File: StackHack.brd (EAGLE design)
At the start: 18.3 x 7.9 mm, 0 parts

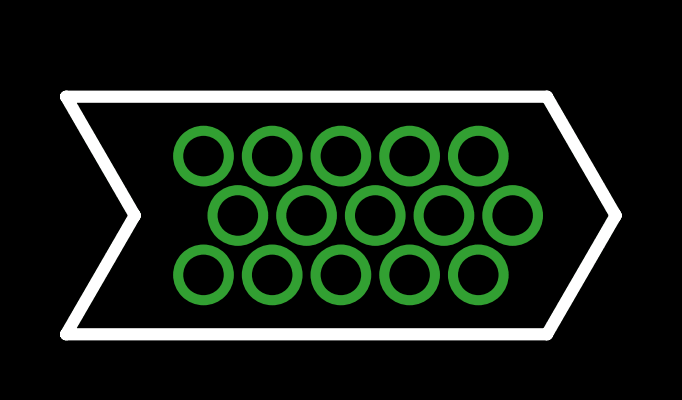
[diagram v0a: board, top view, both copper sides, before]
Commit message: Two VGA's at the same time
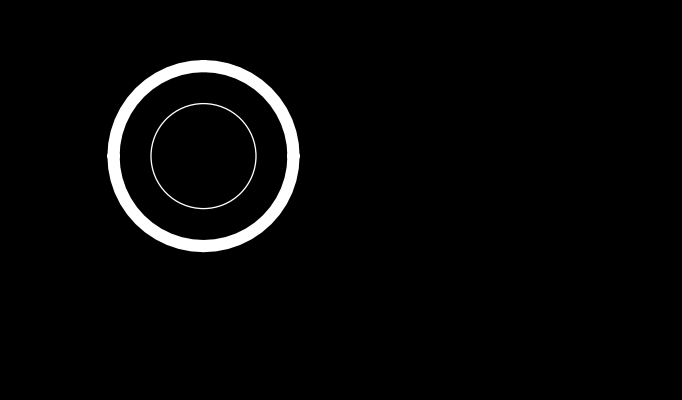
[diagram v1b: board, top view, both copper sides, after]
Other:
- board size 18.3 x 7.9 mm -> 6 x 6 mm
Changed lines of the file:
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@@
 <setting verticaltext="up"/>
 </settings>
-<grid distance="1.98" unitdist="mm" unit="mm" style="lines" multiple="1" display="yes" altdistance="1.98" altunitdist="mm" altunit="mm"/>
+<grid distance="0.5" unitdist="mm" unit="mm" style="lines" multiple="2" display="yes" altdistance="0.1" altunitdist="mm" altunit="mm"/>
 <layers>
 <layer number="1" name="Top" color="4" fill="1" visible="yes" active="yes"/>
@@
 <layer number="43" name="vRestrict" color="2" fill="10" visible="yes" active="yes"/>
 <layer number="44" name="Drills" color="7" fill="1" visible="no" active="yes"/>
-<layer number="45" name="Holes" color="7" fill="1" visible="no" active="yes"/>
+<layer number="45" name="Holes" color="7" fill="1" visible="yes" active="yes"/>
 <layer number="46" name="Milling" color="3" fill="1" visible="no" active="yes"/>
 <layer number="47" name="Measures" color="7" fill="1" visible="no" active="yes"/>
@@
 <board>
 <plain>
-<wire x1="-2.29" y1="-1.98" x2="-4.58" y2="-5.94" width="0.4064" layer="20"/>
-<wire x1="-4.58" y1="1.98" x2="-2.29" y2="-1.98" width="0.4064" layer="20"/>
-<wire x1="13.74" y1="-1.98" x2="11.45" y2="-5.94" width="0.4064" layer="20"/>
-<wire x1="11.45" y1="1.98" x2="13.74" y2="-1.98" width="0.4064" layer="20"/>
-<wire x1="-4.58" y1="1.98" x2="11.45" y2="1.98" width="0.4064" layer="20"/>
-<wire x1="-4.58" y1="-5.94" x2="11.45" y2="-5.94" width="0.4064" layer="20"/>
+<hole x="0" y="0" drill="3.5"/>
+<wire x1="3" y1="0" x2="0" y2="3" width="0.4064" layer="20" curve="90"/>
+<wire x1="0" y1="3" x2="-3" y2="0" width="0.4064" layer="20" curve="90"/>
+<wire x1="-3" y1="0" x2="0" y2="-3" width="0.4064" layer="20" curve="90"/>
+<wire x1="0" y1="-3" x2="3" y2="0" width="0.4064" layer="20" curve="90"/>
 </plain>
 <attributes>
@@
 </elements>
 <signals>
-<signal name="S$1">
-<via x="0" y="0" extent="1-16" drill="1.35"/>
-</signal>
-<signal name="S$2">
-<via x="1.145" y="-1.98" extent="1-16" drill="1.35"/>
-</signal>
-<signal name="S$3">
-<via x="0" y="-3.96" extent="1-16" drill="1.35"/>
-</signal>
-<signal name="S$4">
-<via x="2.29" y="0" extent="1-16" drill="1.35"/>
-</signal>
-<signal name="S$5">
-<via x="4.58" y="0" extent="1-16" drill="1.35"/>
-</signal>
-<signal name="S$6">
-<via x="6.87" y="0" extent="1-16" drill="1.35"/>
-</signal>
-<signal name="S$7">
-<via x="9.16" y="0" extent="1-16" drill="1.35"/>
-</signal>
-<signal name="S$8">
-<via x="2.29" y="-3.96" extent="1-16" drill="1.35"/>
-</signal>
-<signal name="S$9">
-<via x="4.58" y="-3.96" extent="1-16" drill="1.35"/>
-</signal>
-<signal name="S$10">
-<via x="6.87" y="-3.96" extent="1-16" drill="1.35"/>
-</signal>
-<signal name="S$11">
-<via x="9.16" y="-3.96" extent="1-16" drill="1.35"/>
-</signal>
-<signal name="S$12">
-<via x="3.435" y="-1.98" extent="1-16" drill="1.35"/>
-</signal>
-<signal name="S$13">
-<via x="5.725" y="-1.98" extent="1-16" drill="1.35"/>
-</signal>
-<signal name="S$14">
-<via x="8.015" y="-1.98" extent="1-16" drill="1.35"/>
-</signal>
-<signal name="S$15">
-<via x="10.305" y="-1.98" extent="1-16" drill="1.35"/>
-</signal>
 </signals>
 </board>
